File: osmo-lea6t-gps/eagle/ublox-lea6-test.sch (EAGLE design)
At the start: 52 parts, among them U1 UBLOX-LEA-6T, U2 TPS73633, U3 TPS73633, X1 SERIAL, X2 ANT, X3 FOUT, X4 ANT, X5 FOUT, X6 1PPS, X7 PC, X8 1PPS, X9 22-23-2021

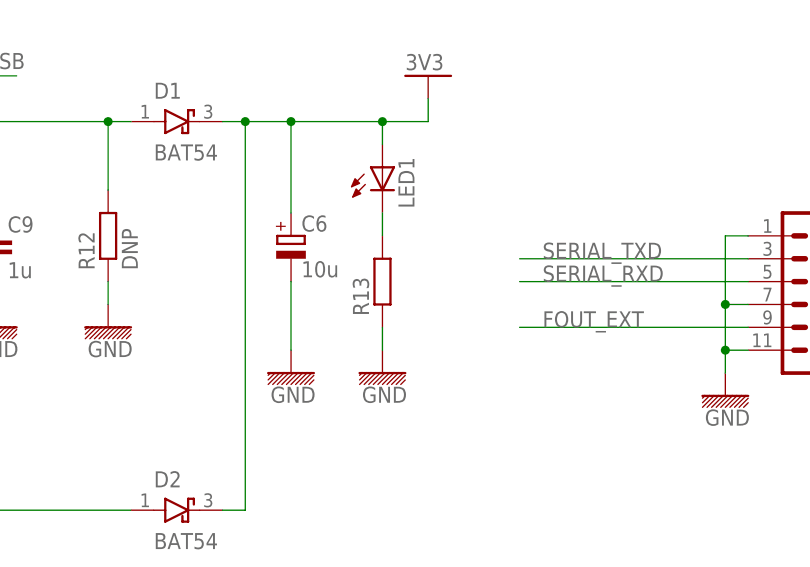
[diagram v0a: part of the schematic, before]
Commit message: Specify LED series resistor as 100 Ohms
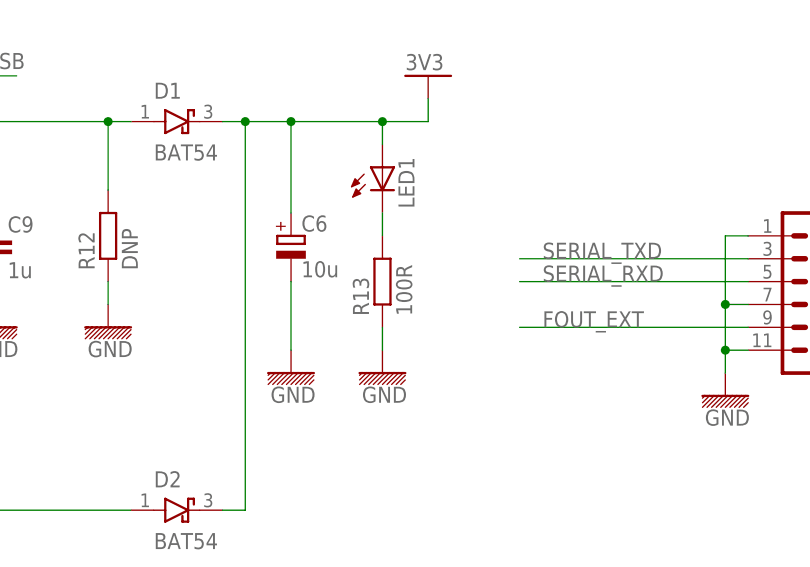
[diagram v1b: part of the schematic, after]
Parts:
- R13: value (none) -> 100R
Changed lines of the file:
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@@
 <part name="U$28" library="we_supply" deviceset="GND" device=""/>
 <part name="LED1" library="led" deviceset="LED" device="SML0603"/>
-<part name="R13" library="we_passive" deviceset="R-EU" device="_0603"/>
+<part name="R13" library="we_passive" deviceset="R-EU" device="_0603" value="100R"/>
 <part name="TP8" library="we_conn" deviceset="TESTPAD" device=""/>
 <part name="R14" library="we_passive" deviceset="R-EU" device="_0603" value="DNP"/>

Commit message: don't put solder cream on SMA edge pads.
The sma edge connectors are hand soldered after the SMT soldering
is already done.  We don't want to have solder paste on them...
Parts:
- X4, X5, X8: device we_conn:SMA-F-S-EDGE -> laforge:SMA-F-S-EDGE
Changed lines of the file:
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@@
 <part name="U$1" library="we_supply" deviceset="GND" device=""/>
 <part name="U$2" library="we_supply" deviceset="GND" device=""/>
-<part name="X4" library="we_conn" deviceset="SMA-F" device="-S-EDGE" value="ANT"/>
-<part name="X5" library="we_conn" deviceset="SMA-F" device="-S-EDGE" value="FOUT"/>
-<part name="X8" library="we_conn" deviceset="SMA-F" device="-S-EDGE" value="1PPS"/>
+<part name="X4" library="laforge" deviceset="SMA-F" device="-S-EDGE" value="ANT"/>
+<part name="X5" library="laforge" deviceset="SMA-F" device="-S-EDGE" value="FOUT"/>
+<part name="X8" library="laforge" deviceset="SMA-F" device="-S-EDGE" value="1PPS"/>
 <part name="U$3" library="we_supply" deviceset="GND" device=""/>
 <part name="U$4" library="we_supply" deviceset="GND" device=""/>
